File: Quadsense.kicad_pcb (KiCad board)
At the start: 2 copper layers, 90 x 90 mm, 45 parts, among them IC1 BME280, IC2 LDO_MCP1801, IC3 ADC_LTC2497, P1 CONN_6, P2 CONN_6, P3 CONN_6, P4 CONN_6, P5 CONN_8, Q1 AO3418

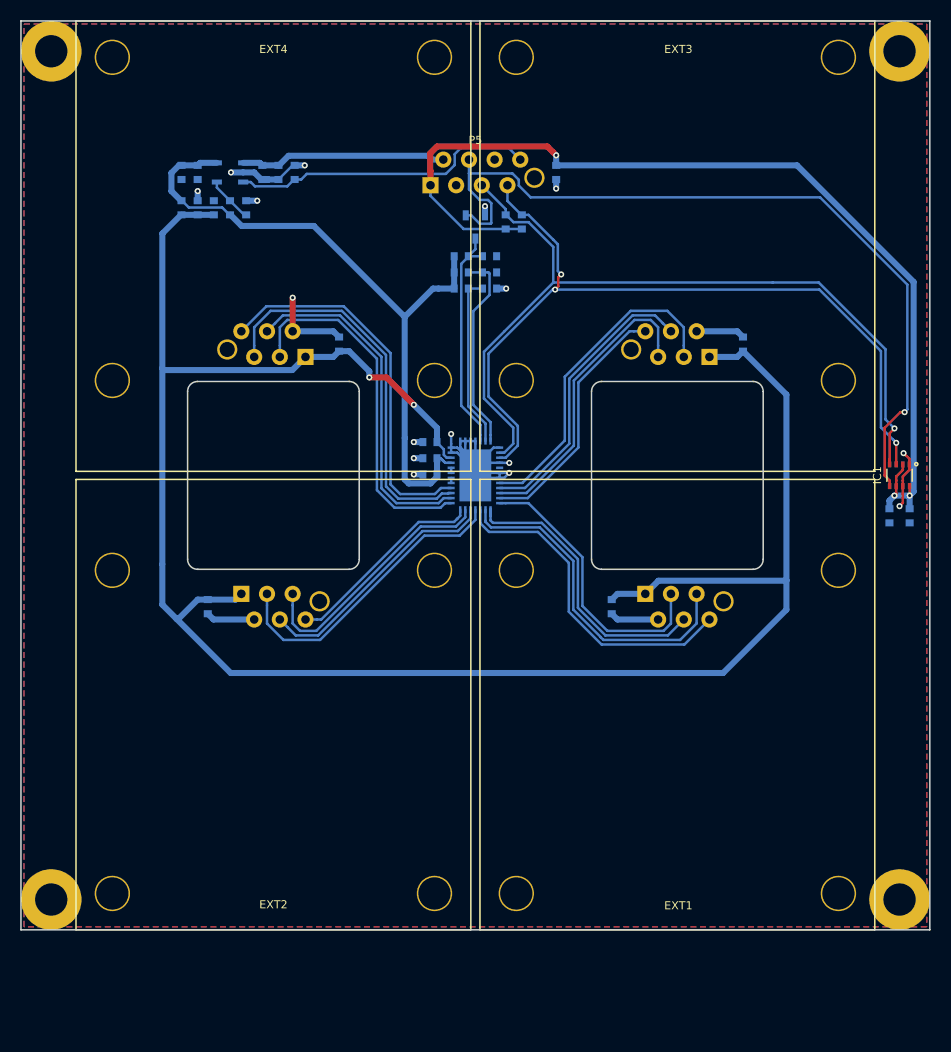
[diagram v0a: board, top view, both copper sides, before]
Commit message: Added second BME280, fixed footprints, better analog decoupling, resized module board
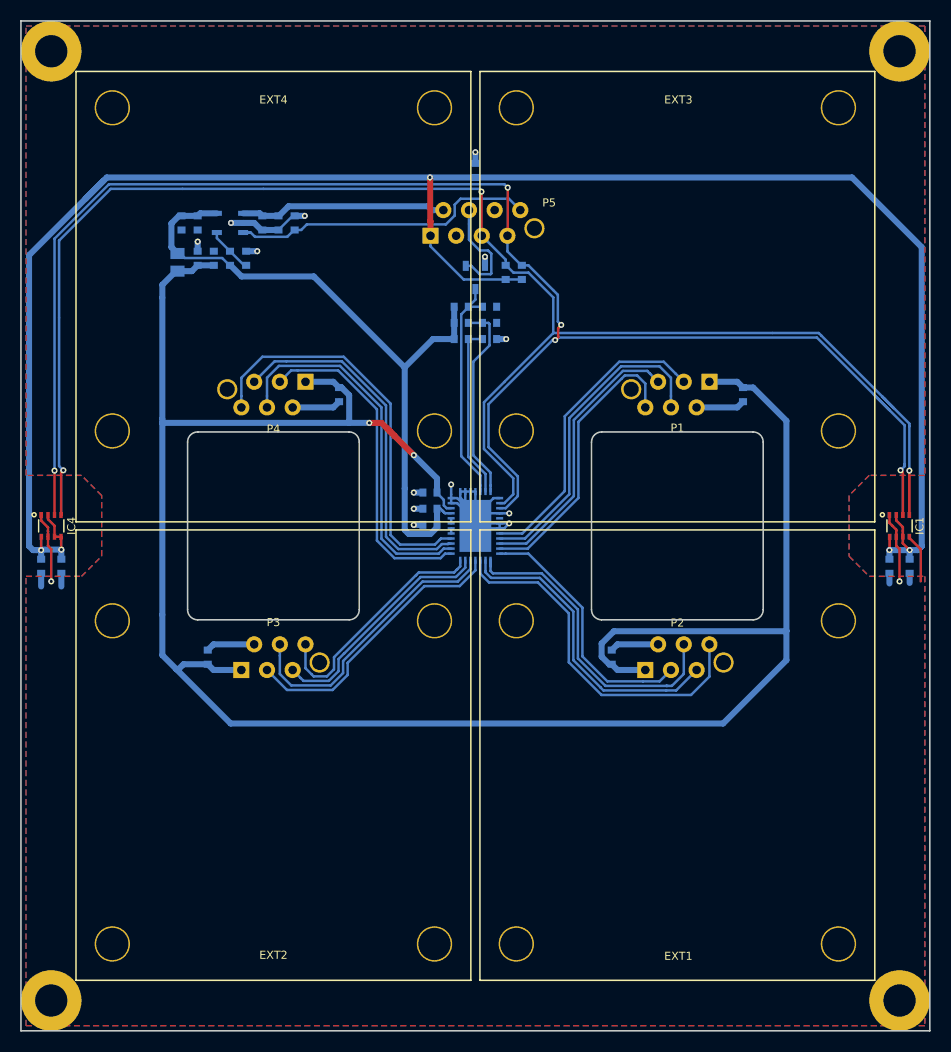
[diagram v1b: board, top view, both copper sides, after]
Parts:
- added C17: 0.1u, everykey:0603, B.Cu at (104.0, 104.0)
- added C18: 0.1u, everykey:0603, B.Cu at (102.0, 104.0)
- added IC4: BME280, everykey:BME280, F.Cu at (103.0, 100.0)
- C12, C13, C14, C15: value C -> 0.1u
- IC2: value LDO_MCP1801 -> AP7330
- L1: value ferrite -> 22u 50mA; footprint everykey:0603 -> everykey:0805
- P1, P2, P3, P4: moved to F.Cu
- R11: value R -> 0/DNP
- moved H2 10.0 mm to (103.0, 147.0)
- moved H3 10.0 mm to (187.0, 147.0)
- moved C11 8.00 mm to (145.0, 64.8), turned to 90 degrees
- moved L1 5.41 mm to (115.5, 73.9)
- moved IC1 5.01 mm to (187.0, 100.0), turned to 90 degrees
- moved C1 5.00 mm to (123.9, 70.0)
- moved C10 5.00 mm to (119.1, 73.5)
- moved C12 5.00 mm to (171.5, 87.0), turned to 90 degrees
- moved C13 5.00 mm to (158.5, 113.0), turned to 270 degrees
- moved C14 5.00 mm to (118.5, 113.0), turned to 270 degrees
- moved C15 5.00 mm to (131.5, 87.0), turned to 90 degrees
- moved C16 5.00 mm to (140.5, 96.7)
- moved C2 5.00 mm to (125.5, 70.0)
- moved C3 5.00 mm to (188.0, 104.0)
- moved C4 5.00 mm to (115.9, 70.0)
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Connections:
- IC1 pad 5: ID1 -> GND
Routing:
- net 3V3: track 98.9 -> 194.7 mm, vias 3 -> 5
- net SDA: track 81.7 -> 164.2 mm, vias 3 -> 5
- net SCL: track 83.3 -> 161.0 mm, vias 1 -> 3
- net ID1: track 80.2 -> 10.6 mm, vias 1 -> 0
- net A4V: track 201.6 -> 216.6 mm
- net GND: track 85.4 -> 99.7 mm, vias 16 -> 15
- net SENS2CH1-: track 20.2 -> 23.9 mm
- net SENS0CH1-: track 25.0 -> 28.6 mm
- net SENS2CH0-: track 25.2 -> 28.6 mm
- net SENS0CH0-: track 28.5 -> 31.8 mm
- net SENS1CH0-: track 29.1 -> 32.1 mm
- net SENS1CH1-: track 32.9 -> 35.8 mm
- net SENS3CH1+: track 38.7 -> 35.9 mm
- net SENS3CH1-: track 37.4 -> 40.1 mm
- net SENS3CH0+: track 35.7 -> 32.9 mm
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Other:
- board size 90 x 90 mm -> 90 x 100 mm

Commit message: Saved files
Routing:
- net GND: track 99.7 -> 143.1 mm, vias 15 -> 19
- net SENS2CH1-: track 23.9 -> 19.2 mm
- net SENS3CH1+: track 35.9 -> 38.6 mm
- net SENS3CH1-: track 40.1 -> 42.3 mm
- net SENS2CH0-: track 28.6 -> 30.6 mm
- net SENS2CH0+: track 28.1 -> 29.9 mm
- net SENS1CH1+: track 30.6 -> 32.4 mm
- net SENS3CH0-: track 37.2 -> 38.8 mm
- net SENS3CH0+: track 32.9 -> 34.5 mm
- net SENS0CH0+: track 30.4 -> 31.8 mm
- net SENS0CH0-: track 31.8 -> 33.2 mm
- net A4V: track 216.6 -> 215.5 mm
- net SENS1CH1-: track 35.8 -> 36.8 mm
- net SENS1CH0-: track 32.1 -> 31.3 mm

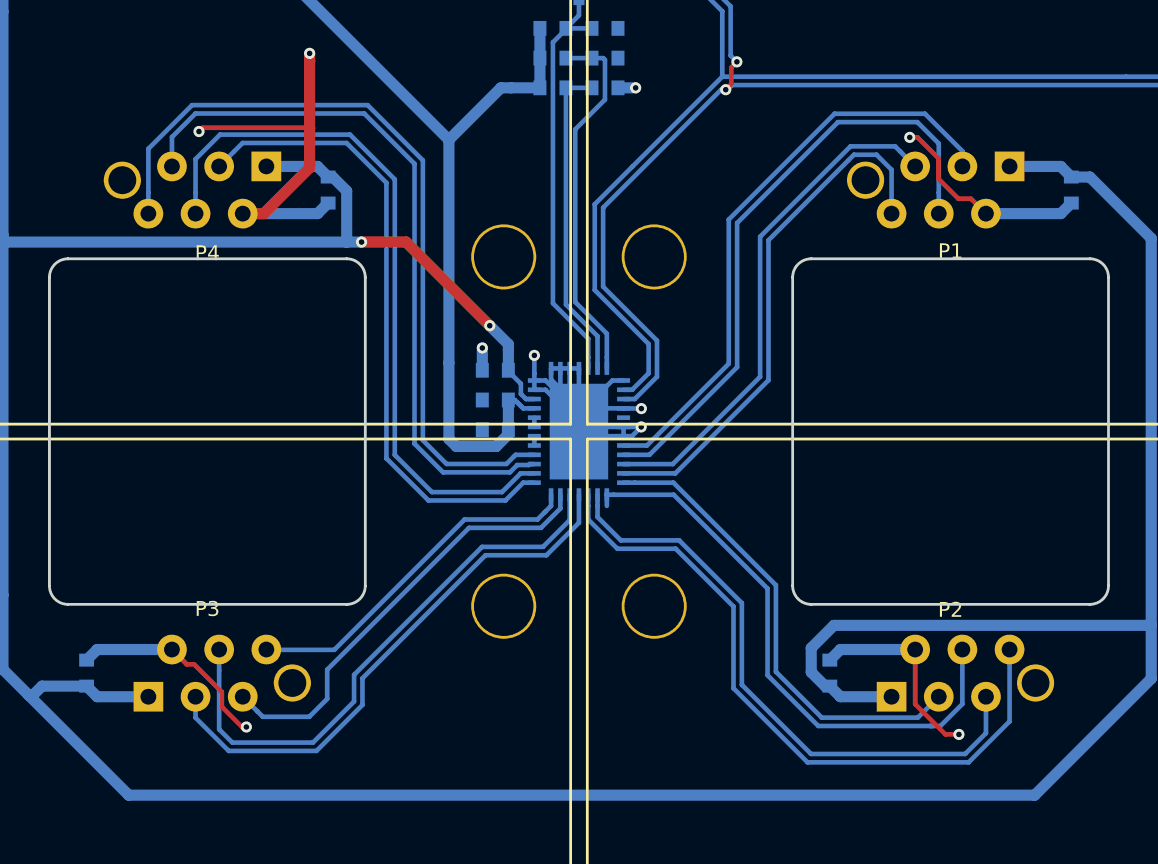
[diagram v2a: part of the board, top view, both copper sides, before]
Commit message: Silkscreen fixes
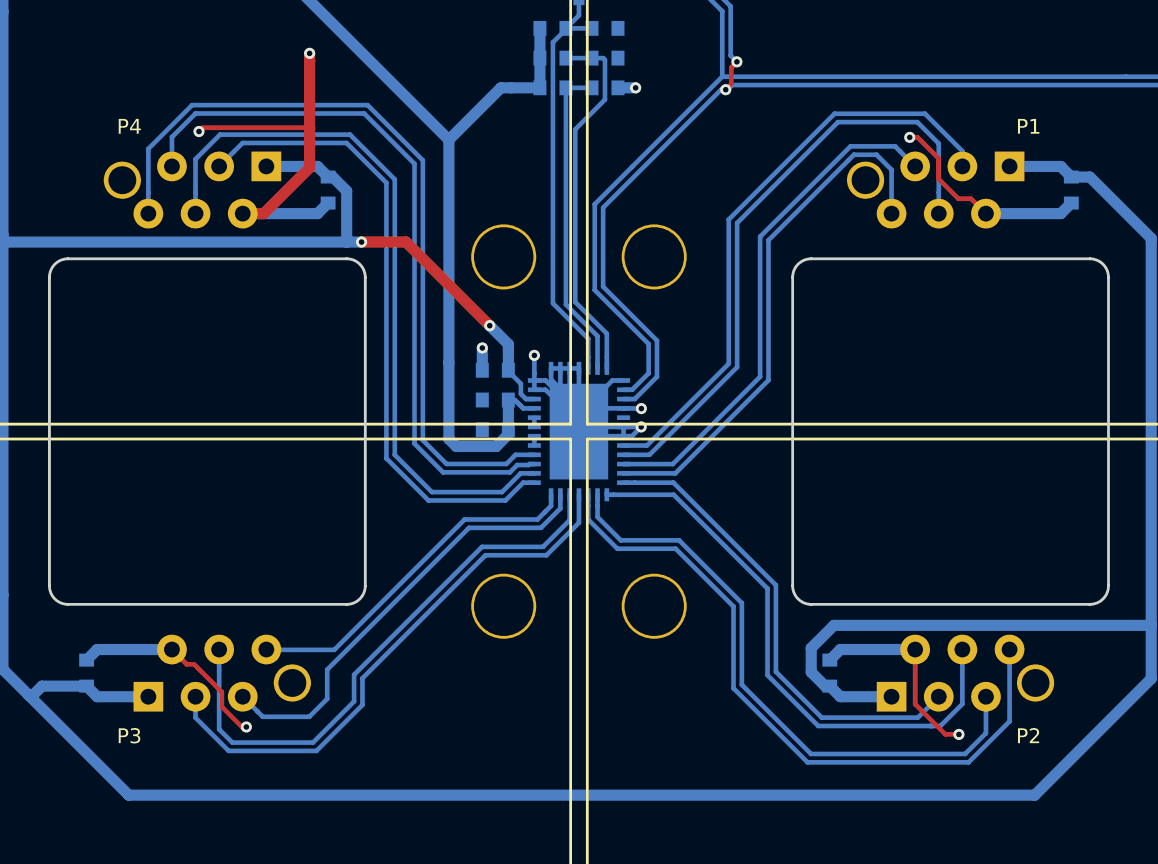
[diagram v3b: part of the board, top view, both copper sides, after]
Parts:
- added LOGO1: Logo, Logo:Logo, B.Cu at (151.8, 122.5)
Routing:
- net SENS1CH0-: track 31.3 -> 30.7 mm
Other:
- board text added: "OpenAir Quadsense V1.1 Made with Love in Cologne by Press Every Key"
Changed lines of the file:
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@@
     (area 99.8 49.425 190.2 150.675)
     (thickness 1.6)
-    (drawings 20)
-    (tracks 555)
+    (drawings 21)
+    (tracks 554)
     (zones 0)
-    (modules 48)
+    (modules 49)
     (nets 32)
   )
@@
   )
   (setup
-    (last_trace_width 0.6)
+    (last_trace_width 0.25)
     (user_trace_width 0.2)
     (user_trace_width 0.25)
@@
     (pad_to_mask_clearance 0.2)
     (aux_axis_origin 100 50)
-    (visible_elements FFFFFFFF)
+    (visible_elements FFFFFF7F)
     (pcbplotparams
       (layerselection 0x010f0_80000001)
@@
       (drillshape 0)
       (scaleselection 1)
-      (outputdirectory Gerber-1.0/))
+      (outputdirectory Gerber-1.1/))
   )
   (net 0 "")
@@
     (at 125 87 180)
     (descr "WR-MM type connector")
-    (fp_text reference P4 (at 0 -3.4 360) (layer F.SilkS)
+    (fp_text reference P4 (at 4.2 3.4 360) (layer F.SilkS)
       (effects (font (size 0.8 0.8) (thickness 0.15)))
     )
@@
     (at 165 87 180)
     (descr "WR-MM type connector")
-    (fp_text reference P1 (at 0 -3.3 360) (layer F.SilkS)
+    (fp_text reference P1 (at -4.2 3.4 360) (layer F.SilkS)
       (effects (font (size 0.8 0.8) (thickness 0.15)))
     )
@@
     (at 165 113)
     (descr "WR-MM type connector")
-    (fp_text reference P2 (at 0 -3.4 180) (layer F.SilkS)
+    (fp_text reference P2 (at 4.2 3.4 180) (layer F.SilkS)
       (effects (font (size 0.8 0.8) (thickness 0.15)))
     )
@@
     (at 125 113)
     (descr "WR-MM type connector")
-    (fp_text reference P3 (at 0 -3.45 180) (layer F.SilkS)
+    (fp_text reference P3 (at -4.2 3.4 180) (layer F.SilkS)
       (effects (font (size 0.8 0.8) (thickness 0.15)))
     )
@@
     (descr 0805)
     (tags 0805)
-    (fp_text reference L1 (at -2 0 540) (layer B.SilkS)
-      (effects (font (size 0.8 0.8) (thickness 0.15)) (justify mirror))
-    )
-    (fp_text value "22u 50mA" (at 0 -1.5 270) (layer B.Fab)
+    (fp_text reference L1 (at 2.4 0 270) (layer B.SilkS)
+      (effects (font (size 0.8 0.8) (thickness 0.15)) (justify mirror))
+    )
+    (fp_text value "22u 50mA" (at 0 -1.5 270) (layer B.Fab) hide
       (effects (font (size 0.8 0.8) (thickness 0.15)) (justify mirror))
     )
@@
     (pad 2 smd rect (at 0.875 0 270) (size 1.1 1.4) (layers B.Cu B.Paste B.Mask)
       (net 31 A4V))
+  )
+  (module Logo:Logo (layer B.Cu)
+    (at 151.8 122.5 180)
+    (fp_text reference LOGO1 (at 0 0 180) (layer B.SilkS) hide
+      (effects (font (thickness 0.3)) (justify mirror))
+    )
+    (fp_text value Logo (at 0.75 0 180) (layer B.SilkS) hide
+      (effects (font (thickness 0.3)) (justify mirror))
+    )
+    (fp_poly (pts (xy -1.530848 3.031431) (xy -1.508561 3.022361) (xy -1.111712 2.787847) (xy -0.708354 2.427093)
+      (xy -0.337123 1.977064) (xy -0.200391 1.770825) (xy 0.10318 1.279001) (xy 0.559477 1.536519)
+      (xy 1.132146 1.769543) (xy 1.732443 1.852062) (xy 2.328405 1.787403) (xy 2.88807 1.578894)
+      (xy 3.363607 1.244576) (xy 3.571023 1.015549) (xy 3.788405 0.714256) (xy 3.988355 0.386914)
+      (xy 4.143478 0.079738) (xy 4.226379 -0.161057) (xy 4.233266 -0.222476) (xy 4.315712 -0.276951)
+      (xy 4.554335 -0.320705) (xy 4.936191 -0.351462) (xy 4.978931 -0.353601) (xy 5.398852 -0.38446)
+      (xy 5.698325 -0.436466) (xy 5.925892 -0.519952) (xy 6.028251 -0.576959) (xy 6.354536 -0.87025)
+      (xy 6.542348 -1.260194) (xy 6.590738 -1.744651) (xy 6.585092 -1.835526) (xy 6.50339 -2.25957)
+      (xy 6.320949 -2.582256) (xy 6.010423 -2.842632) (xy 5.795266 -2.963333) (xy 5.376333 -3.175)
+      (xy 0.254 -3.19471) (xy -0.813852 -3.198507) (xy -1.725961 -3.200833) (xy -2.495916 -3.201375)
+      (xy -3.137302 -3.199817) (xy -3.663708 -3.195844) (xy -4.08872 -3.189142) (xy -4.425926 -3.179395)
+      (xy -4.688913 -3.166288) (xy -4.891268 -3.149507) (xy -5.046578 -3.128737) (xy -5.168431 -3.103662)
+      (xy -5.270413 -3.073968) (xy -5.293437 -3.06612) (xy -5.825119 -2.824948) (xy -6.207588 -2.521163)
+      (xy -6.442673 -2.167376) (xy -6.581081 -1.696312) (xy -6.570896 -1.494511) (xy -6.149721 -1.494511)
+      (xy -6.117962 -1.873093) (xy -5.933879 -2.203835) (xy -5.610516 -2.475327) (xy -5.160918 -2.67616)
+      (xy -4.674397 -2.784932) (xy -4.470304 -2.801061) (xy -4.122245 -2.813845) (xy -3.649413 -2.82344)
+      (xy -3.071002 -2.83) (xy -2.406206 -2.833682) (xy -1.674218 -2.83464) (xy -0.894233 -2.833031)
+      (xy -0.085443 -2.82901) (xy 0.732958 -2.822732) (xy 1.541776 -2.814353) (xy 2.321817 -2.804029)
+      (xy 3.053887 -2.791914) (xy 3.718794 -2.778164) (xy 4.297343 -2.762935) (xy 4.77034 -2.746382)
+      (xy 5.118593 -2.728661) (xy 5.322907 -2.709928) (xy 5.354968 -2.703687) (xy 5.748566 -2.531114)
+      (xy 6.026145 -2.268118) (xy 6.167126 -1.937507) (xy 6.180667 -1.788496) (xy 6.136743 -1.391219)
+      (xy 5.995822 -1.099951) (xy 5.744175 -0.90542) (xy 5.368075 -0.798349) (xy 4.853796 -0.769465)
+      (xy 4.679496 -0.774278) (xy 3.961045 -0.804333) (xy 3.815366 -0.338666) (xy 3.651586 0.124112)
+      (xy 3.476076 0.471976) (xy 3.25765 0.758223) (xy 3.059474 0.953229) (xy 2.603419 1.258285)
+      (xy 2.092476 1.416035) (xy 1.554336 1.427006) (xy 1.016691 1.291723) (xy 0.507231 1.010714)
+      (xy 0.368778 0.902092) (xy 0.173909 0.75986) (xy 0.016905 0.682797) (xy -0.012222 0.678215)
+      (xy -0.103176 0.750094) (xy -0.231588 0.937753) (xy -0.369764 1.200673) (xy -0.370631 1.202535)
+      (xy -0.644457 1.677178) (xy -0.987456 2.098906) (xy -1.366231 2.434659) (xy -1.74738 2.651376)
+      (xy -1.876803 2.693402) (xy -2.298205 2.751855) (xy -2.70811 2.697041) (xy -3.162874 2.520567)
+      (xy -3.217333 2.493729) (xy -3.691748 2.178537) (xy -4.016207 1.786087) (xy -4.189104 1.32076)
+      (xy -4.208839 0.78694) (xy -4.073805 0.189008) (xy -4.067474 0.170493) (xy -3.975942 -0.154421)
+      (xy -3.984042 -0.358134) (xy -4.107653 -0.466614) (xy -4.362652 -0.50583) (xy -4.482333 -0.508)
+      (xy -4.91511 -0.546427) (xy -5.338023 -0.650098) (xy -5.696241 -0.801599) (xy -5.917412 -0.963815)
+      (xy -6.058137 -1.188717) (xy -6.145463 -1.464999) (xy -6.149721 -1.494511) (xy -6.570896 -1.494511)
+      (xy -6.559244 -1.263672) (xy -6.384155 -0.881316) (xy -6.062806 -0.561102) (xy -5.602189 -0.314891)
+      (xy -5.291743 -0.215243) (xy -4.997218 -0.144939) (xy -4.751514 -0.097535) (xy -4.635042 -0.084666)
+      (xy -4.538088 -0.062757) (xy -4.51405 0.033202) (xy -4.546997 0.232834) (xy -4.620151 0.892609)
+      (xy -4.553617 1.496477) (xy -4.35195 2.025506) (xy -4.019705 2.460763) (xy -4.008254 2.471714)
+      (xy -3.582661 2.780813) (xy -3.075187 3.001673) (xy -2.532768 3.123957) (xy -2.002343 3.137322)
+      (xy -1.530848 3.031431)) (layer B.SilkS) (width 0.01))
+  )
+  (gr_text "OpenAir Quadsense V1.1\nMade with Love in Cologne\nby Press Every Key" (at 158.1 130.3) (layer B.SilkS)
+    (effects (font (size 1.5 1.5) (thickness 0.3)) (justify left mirror))
   )
   (gr_arc (start 172.5 108.3) (end 173.5 108.3) (angle 90) (layer Edge.Cuts) (width 0.15))
@@
   (segment (start 165.635 114.665002) (end 164.454991 115.845011) (width 0.25) (layer B.Cu) (net 9))
   (segment (start 164.454991 115.845011) (end 163.9 115.845011) (width 0.25) (layer B.Cu) (net 9))
-  (segment (start 146.5 104) (end 146.5 103.4) (width 0.25) (layer B.Cu) (net 9))
   (segment (start 146.5 103.26359) (end 146.5 103.4) (width 0.25) (layer B.Cu) (net 9))
   (segment (start 146 104) (end 146 103.4) (width 0.25) (layer B.Cu) (net 10))
